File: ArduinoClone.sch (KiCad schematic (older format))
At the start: 13 parts, among them U1 DS1337S+, U2 24LC1025, U3 24LC1025, U4 ATMEGA328-AU, Y1 Crystal 32MHz, Y2 Crystal 16MHz

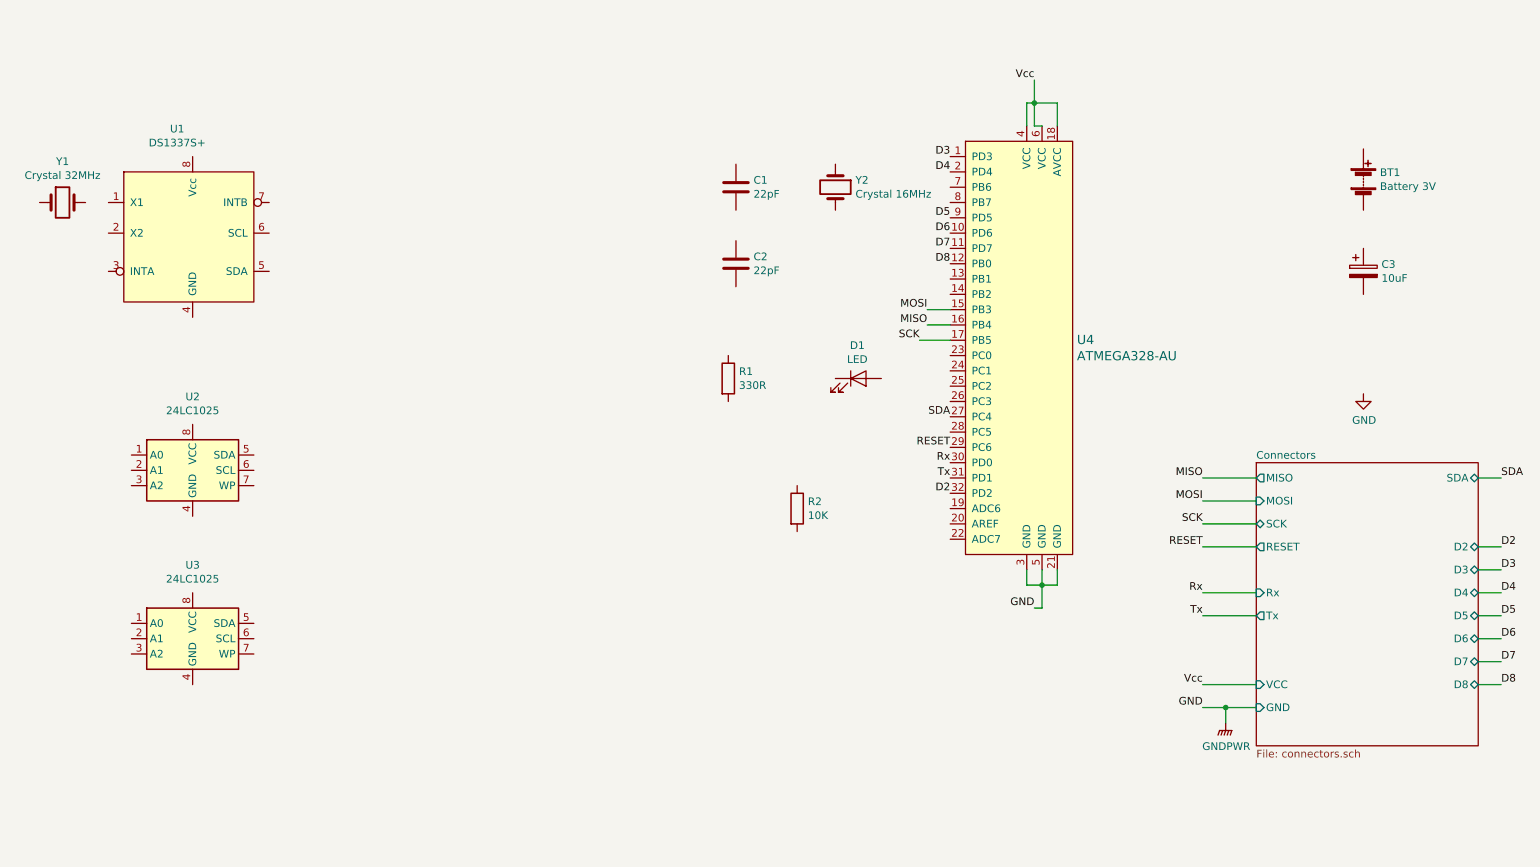
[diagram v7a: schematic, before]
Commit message: Completed wiring in the root sheet
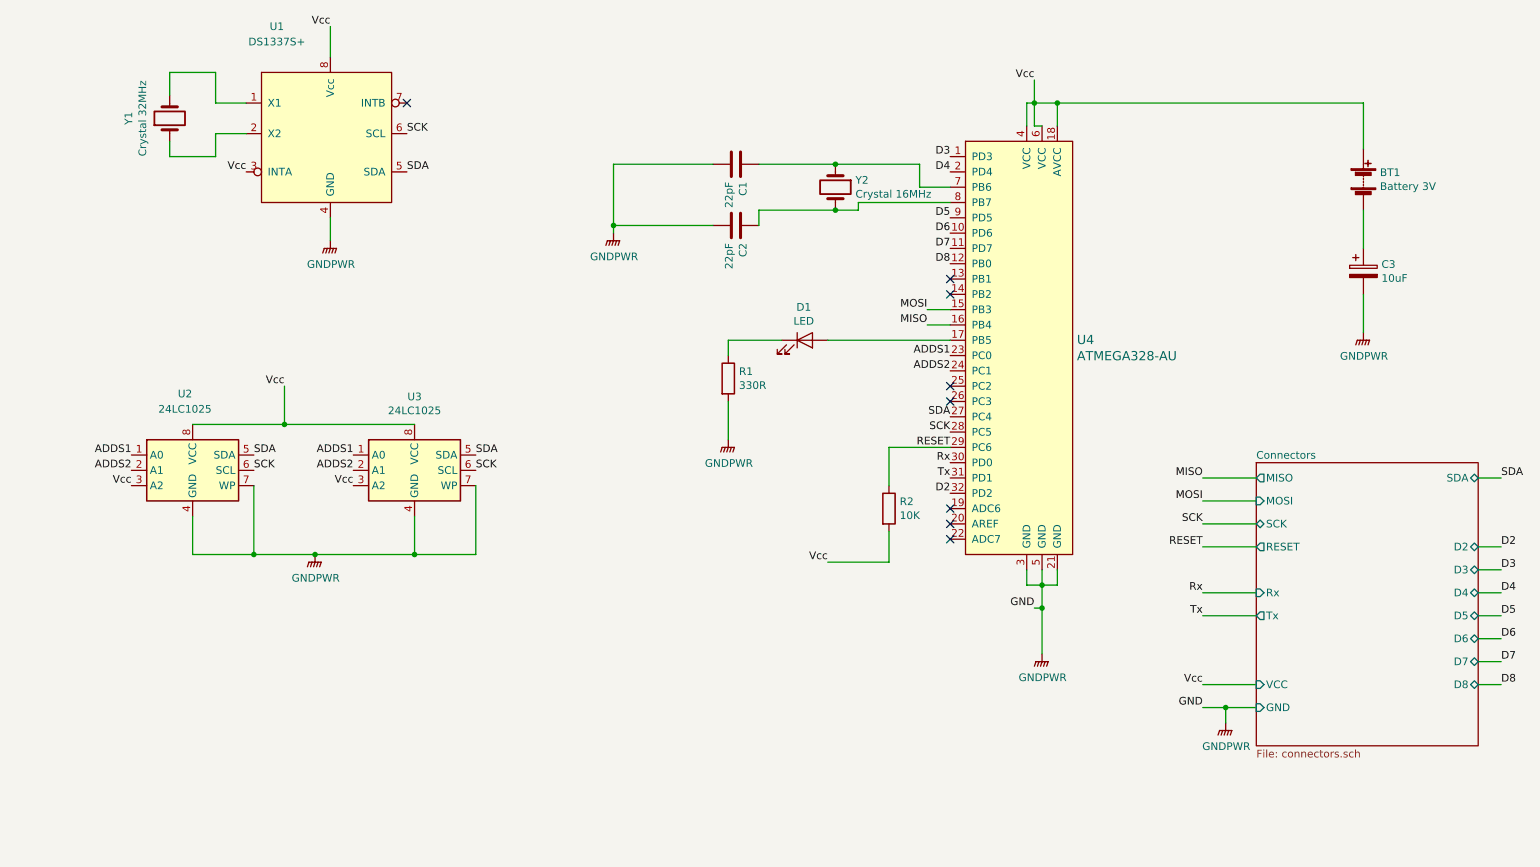
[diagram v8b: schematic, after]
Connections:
- net GND is gone; now on net GNDPWR: U4.21 (GND), U4.3 (GND), U4.5 (GND)
- net RESET: now also R2.1
- net SCK: now also U1.6 (SCL), U2.6 (SCL), U3.6 (SCL), U4.28 (PC5); no longer U4.17 (PB5)
- net SDA: now also U1.5 (SDA), U2.5 (SDA), U3.5 (SDA)
- net Vcc: now also BT1.1 (+), R2.2, U1.3 (INTA), U1.8 (Vcc), U2.3 (A2), U2.8 (VCC), U3.3 (A2), U3.8 (VCC)
- net at BT1.2 (-): now also C3.1
- net at C1.1: now also U4.7 (PB6), Y2.1
- net GNDPWR: now reaches C1.2
- net GNDPWR: now also C2.2, C3.2, R1.2, U1.4 (GND), U2.4 (GND), U2.7 (WP), U3.4 (GND), U3.7 (WP)
- net at C2.1: now also U4.8 (PB7), Y2.2
- net at D1.1 (K): now also R1.1
- net at D1.2 (A): now also U4.17 (PB5)
- net ADDS1: now reaches U2.1 (A0)
- net ADDS1: now also U3.1 (A0), U4.23 (PC0)
- net ADDS2: now reaches U2.2 (A1)
- net ADDS2: now also U3.2 (A1), U4.24 (PC1)
- net at U1.1 (X1): now also Y1.2
- net at U1.2 (X2): now also Y1.1
- no-connect marks 0 -> 8
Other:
- moved on the sheet: C1, C2, D1, R2, U1, U3, Y1
